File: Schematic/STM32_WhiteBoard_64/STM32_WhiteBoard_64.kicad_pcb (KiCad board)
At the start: 2 copper layers, 25.6 x 65 mm, 62 parts, among them J1 SWDIO+Serial, J2 USB_B_Micro, J3 Header1, J4 Header2, Q1 BC847BS, Q2 Si3493DDV, Q3 BC857BS, SW1 Boot0, SW2 Reset, SW3 SW_DIP_x01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

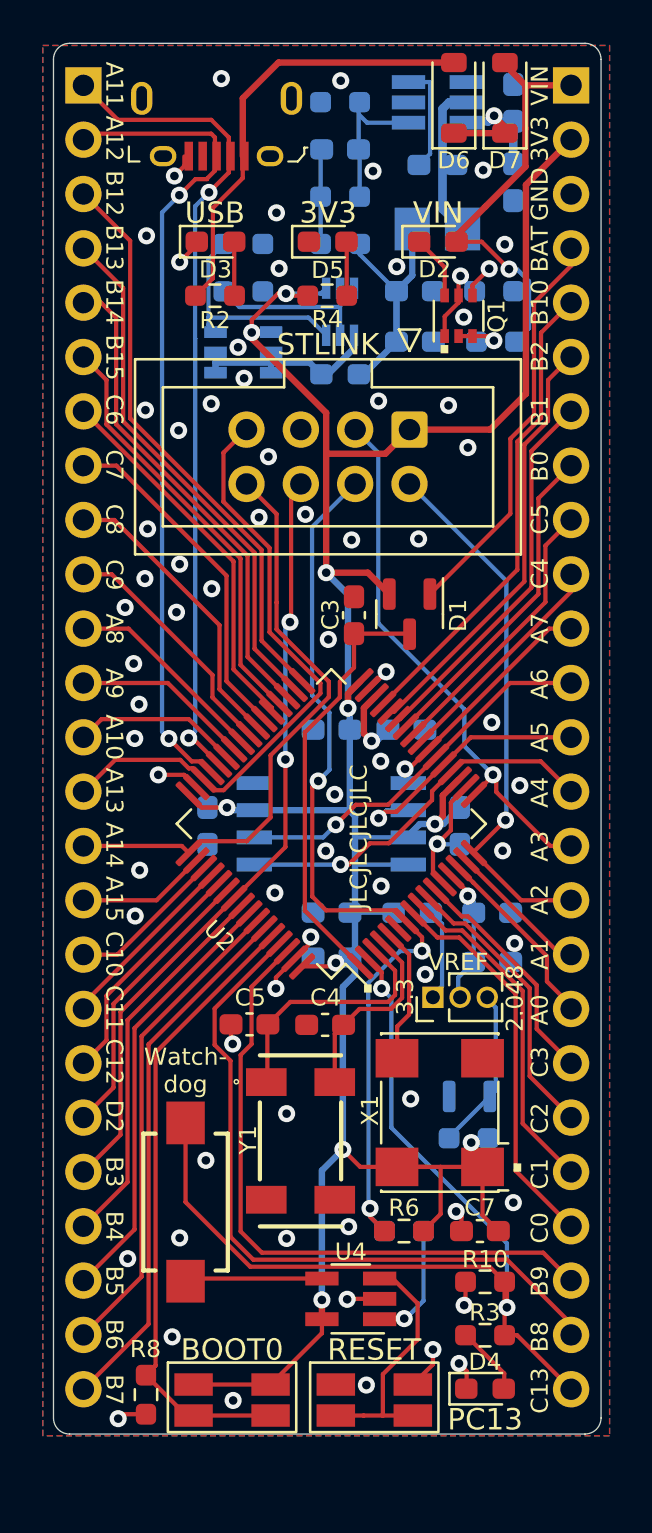
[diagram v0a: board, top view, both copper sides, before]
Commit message: Added btn PD2, added fuse, removed hardware watchdog
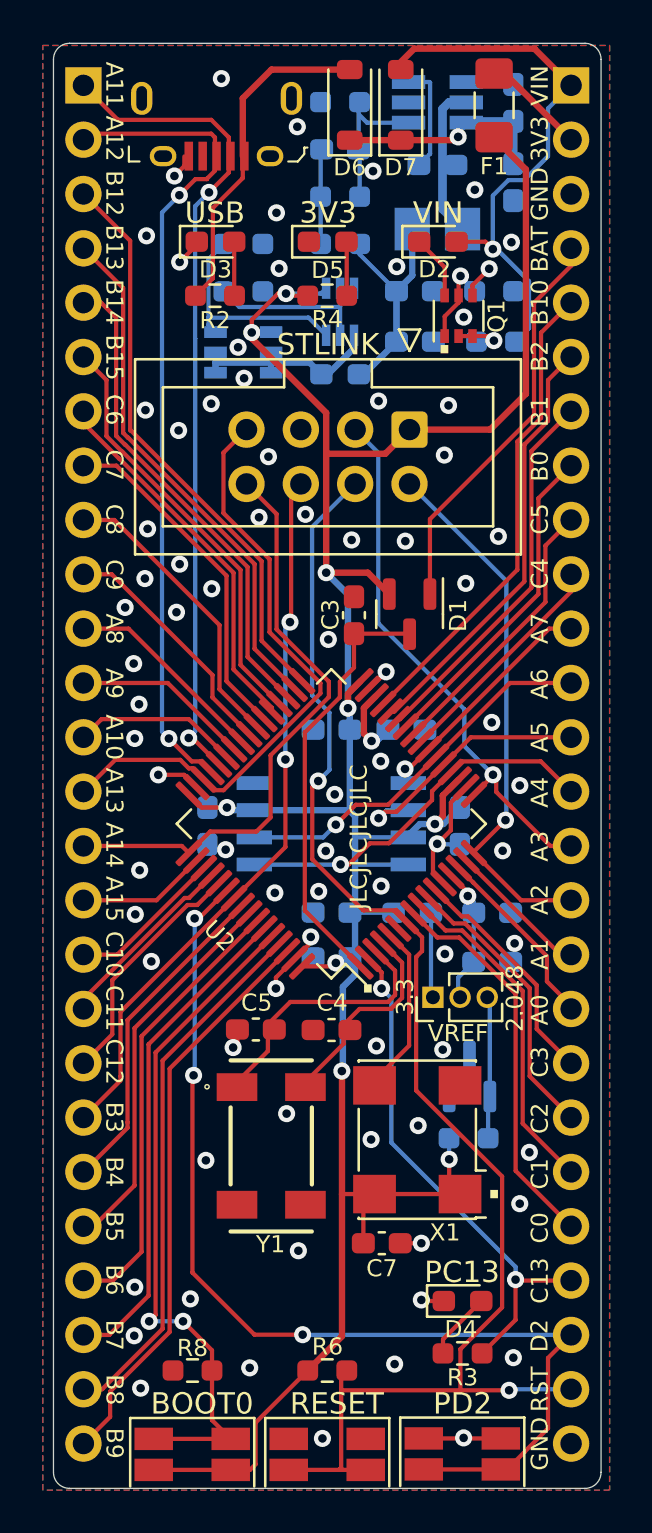
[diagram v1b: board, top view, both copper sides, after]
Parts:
- removed the R10 at (193.2, 136.3)
- removed the R9 at (189.4, 133.9)
- removed the U4 at (186.9, 137.1)
- added F1: 1A, Fuse:Fuse_1206_3216Metric_Pad1.42x1.75mm_HandSolder, F.Cu at (193.6, 81.3)
- J3: renamed from J4; footprint Connector_PinHeader_2.54mm:PinHeader_1x25_P2.54mm_Vertical -> Connector_PinHeader_2.54mm:PinHeader_1x26_P2.54mm_Vertical
- J4: renamed from J3; footprint Connector_PinHeader_2.54mm:PinHeader_1x25_P2.54mm_Vertical -> Connector_PinHeader_2.54mm:PinHeader_1x26_P2.54mm_Vertical
- SW3: value SW_DIP_x01 -> User; footprint Retronics_Switches:CFS0102TA -> myDevices:PTS840ESDGMSMTRLFS
- Y1: footprint SamacSys_Parts:ABS25 -> SamacSys_Parts:ABS25-Retronics22
- moved SW3 17.5 mm to (192.1, 144.3), turned to 0 degrees
- moved R6 7.44 mm to (185.8, 140.4), turned to 180 degrees
- moved D6 4.88 mm to (186.8, 81.3)
- moved D7 4.88 mm to (189.2, 81.3)
- moved C7 4.62 mm to (188.3, 134.5), turned to 0 degrees
- moved D4 4.23 mm to (192.1, 137.2)
- moved SW2 3.36 mm to (185.8, 144.4)
- moved SW1 3.15 mm to (179.5, 144.4)
- moved R8 2.45 mm to (179.5, 140.4), turned to 0 degrees
- moved X1 1.65 mm to (190.0, 129.7)
- moved Y1 1.39 mm to (183.2, 129.9)
- moved R3 1.35 mm to (192.1, 139.7)
- moved C4 0.38 mm to (186.0, 124.5)
- moved C5 0.38 mm to (182.5, 124.5)
- turned R1 to 0 degrees
- renumbered R12 to R10, R13 to R11, R14 to R12, R15 to R13, R11 to R9, U5 to U4
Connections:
- J3 pad 20: /PD2 -> /PB3
- J3 pad 21: /PB3 -> /PB4
- J3 pad 22: /PB4 -> /PB5
- J3 pad 23: /PB5 -> /PB6
- J3 pad 24: /PB6 -> /PB7
- J3 pad 25: /PB7 -> /PB8
- J4 pad 2: +3.3V -> Net-(J4-Pin_2)
- J4 pad 23: /PB9 -> /PC13
- J4 pad 24: /PB8 -> /PD2
- J4 pad 25: /PC13 -> /~{RESET}
- SW1 pad 1: +3.3V -> /BOOT0
- SW1 pad 2: /BOOT0 -> +3.3V
- SW2 pad 2: /~{MR} -> /~{RESET}
- SW3 pad 1: /PC13 -> GND
- SW3 pad 2: Net-(U4-WDI) -> /PD2
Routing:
- net /PD2: track 13.4 -> 49.0 mm, vias 0 -> 3
- net /~{RESET}: track 43.8 -> 68.7 mm, vias 3 -> 2
- net /PC13: track 47.0 -> 24.6 mm
- net /~{MR}: track 11.8 -> 0.00 mm
- net /PB8: track 33.4 -> 25.1 mm
- net Net-(U4-WDI): track 6.55 -> 0.00 mm
- net VCC: track 19.2 -> 25.8 mm
- net Net-(U4-~{RESET}): track 5.67 -> 0.00 mm, vias 1 -> 0
- net VBUS: track 20.7 -> 15.7 mm
- net Net-(J4-Pin_2): track 0.00 -> 4.88 mm
- net GND: track 27.2 -> 23.3 mm, vias 71 -> 79
- net /PB9: track 30.4 -> 27.0 mm
- net /PB3: track 36.4 -> 33.8 mm
- net /PB4: track 18.0 -> 15.5 mm
- net Net-(D6-K): track 7.67 -> 10.2 mm
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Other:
- board size 25.6 x 65 mm -> 25.6 x 67.6 mm
- board text added: "PD2"
- board text added: "RST"
- board text added: "STM32_WhiteBoard_64 R0144C_Pb_2340 Bjørner Sandom"
- board text removed: "STM32_WhiteBoard_64 R0144C_Pb_2339 Bjørner Sandom"
- board text removed: "Watch- dog"
